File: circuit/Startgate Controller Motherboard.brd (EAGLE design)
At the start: 50 x 100 mm, 11 parts, among them IC1 MAX3490ESA, IC2 L293D, U1 PROMINI, U2 TCA9548A, X1 RJ45-8L21-B, X2 SOLENOID

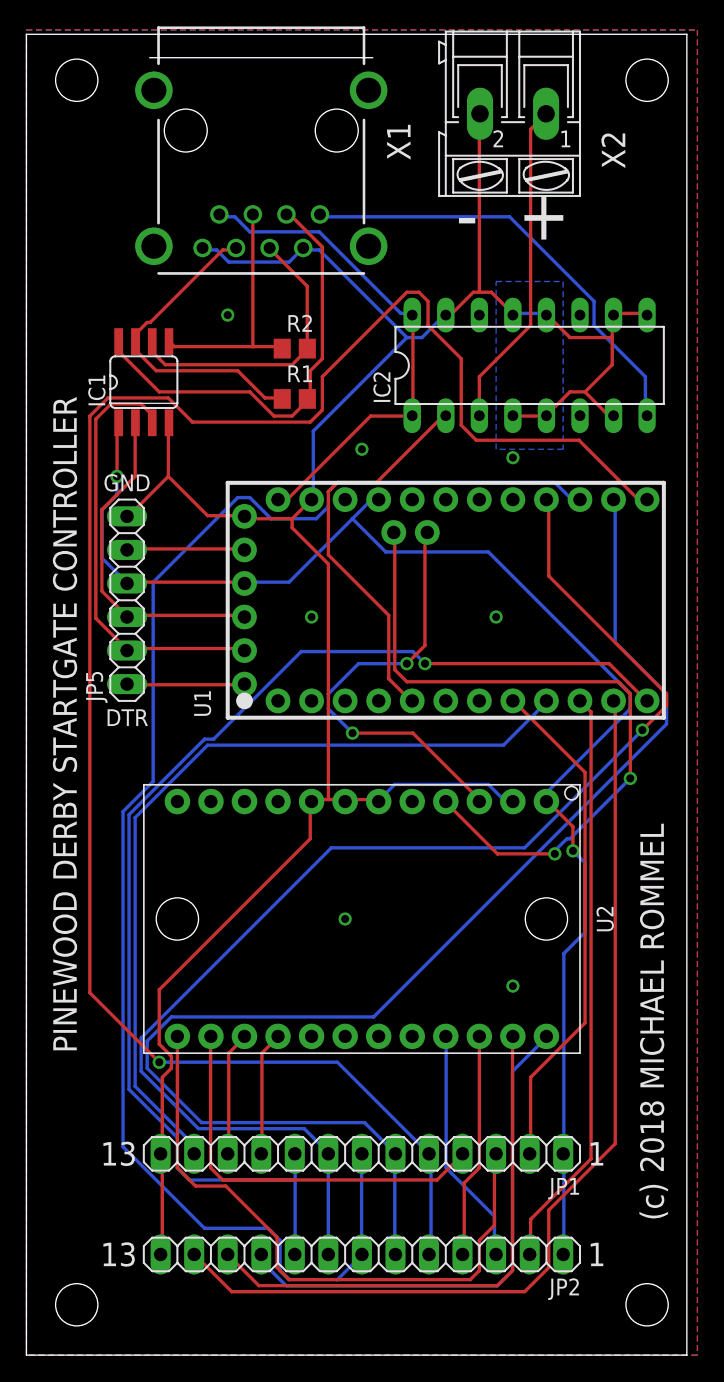
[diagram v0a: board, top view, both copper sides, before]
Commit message: create the final schematics and boards
Some schematics errors have been corrected. Another connector for
the laser diodes of the Finishing Gate has been added. The
connectors to the daughterboards have been rotated, so that the
cabling will run mostly straight.

All gerber files have been added as well as .zip files for the
boardhouse.
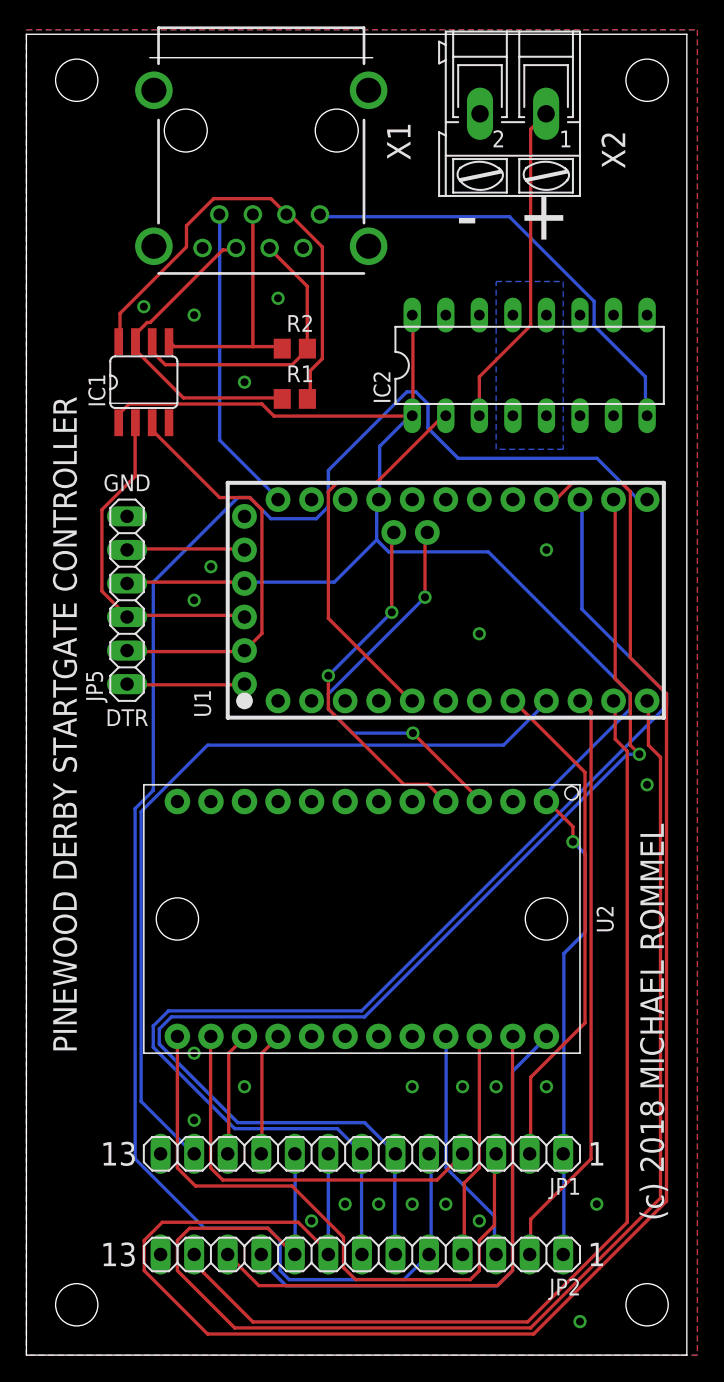
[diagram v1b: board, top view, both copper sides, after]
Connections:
- net +3V3: now also IC2.1, IC2.16
- net +5V: no longer IC2.1, IC2.16
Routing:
- net GND: track 185.3 -> 0.00 mm, vias 7 -> 24
- net SCK: track 96.6 -> 133.2 mm, vias 1 -> 0
- net N$5: track 53.5 -> 27.2 mm
- net +3V3: track 108.8 -> 133.2 mm, vias 2 -> 1
- net MISO: track 113.7 -> 95.7 mm
- net +5V: track 38.2 -> 23.4 mm
- net SS: track 141.7 -> 130.9 mm, vias 1 -> 0
- net RST: track 91.0 -> 100.5 mm, vias 1 -> 0
- net ENA4: track 73.8 -> 78.3 mm
- net MOSI: track 99.1 -> 95.2 mm, vias 0 -> 1
- net N$3: track 33.5 -> 35.6 mm
- net N$6: track 33.1 -> 30.9 mm
- net N$1: track 33.3 -> 31.5 mm
